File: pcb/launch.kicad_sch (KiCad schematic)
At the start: 243 parts, among them J1 DNP, J6 DNP, U1 AT90USB646-MUR, Y0 ECS-160-18-23G-JGN-TR

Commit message: work in progress toward 2.0
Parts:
- added J7: FH12-16S-0.5SH(55), Connector_FFC-FPC:Hirose_FH12-16S-0.5SH_1x16-1MP_P0.50mm_Horizontal, symbol Connector_Generic_MountingPin:Conn_01x16_MountingPin
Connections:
- net +3V6: now also J7.14 (Pin_14), J7.15 (Pin_15)
- net COLD: now also J7.12 (Pin_12)
- net COLE: now also J7.11 (Pin_11)
- net COLF: now also J7.10 (Pin_10)
- net COLM: now also J7.9 (Pin_9)
- net GND: now also J7.1 (Pin_1), J7.16 (Pin_16), J7.8 (Pin_8), J7.MP (MountPin)
- net LED_TEN: now reaches LO0.3 (DOUT)
- net LED_TEN: now also J7.13 (Pin_13)
- net ROW6: now reaches U1.27 (PD2)
- net ROW6: now also J7.2 (Pin_2)
- net ROW7: now reaches U1.29 (PD4)
- net ROW7: now also J7.3 (Pin_3)
- net ROW8: now reaches U1.30 (PD5)
- net ROW8: now also J7.4 (Pin_4)
- net ROW9: now reaches U1.31 (PD6)
- net ROW9: now also J7.5 (Pin_5)
- net ROW10: now reaches U1.32 (PD7)
- net ROW10: now also J7.6 (Pin_6)
- net ROW11: now reaches U1.33 (PE0)
- net ROW11: now also J7.7 (Pin_7)
- no-connect marks 3 -> 2
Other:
- sheet power ports: added none; removed ~{RESET}
- note added: "Tenkey connector"

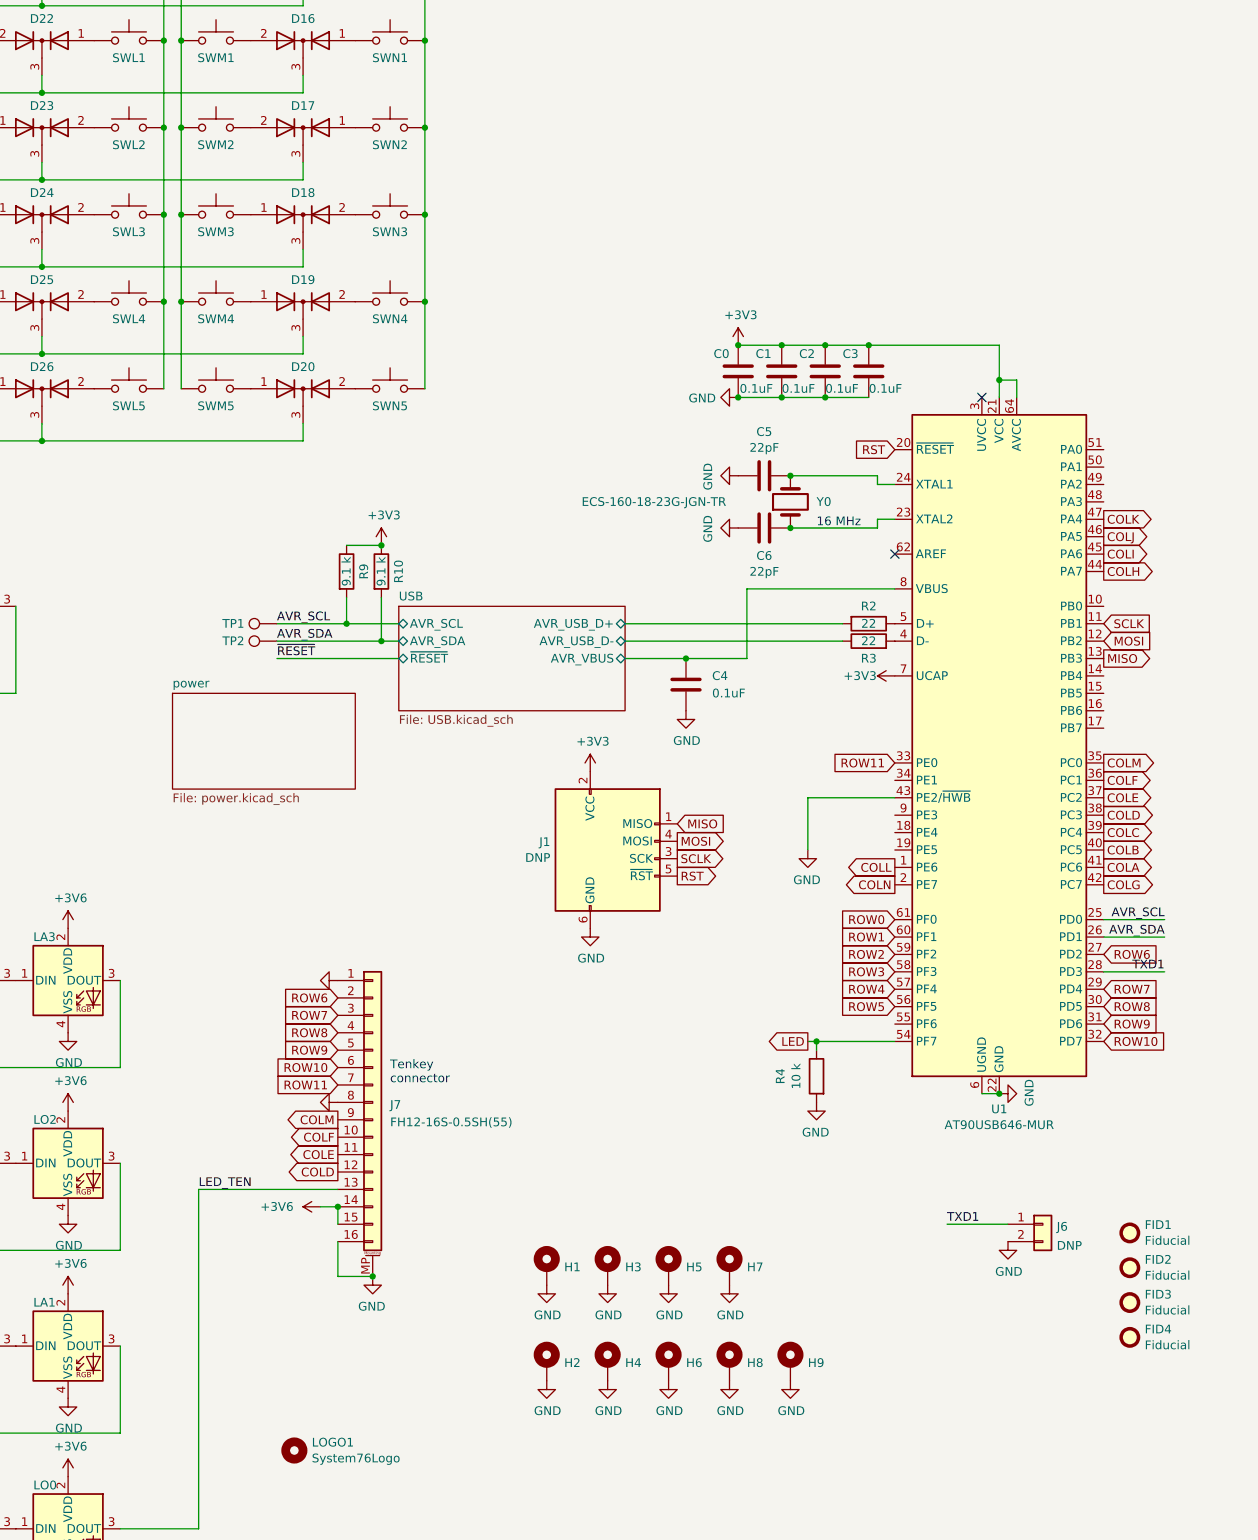
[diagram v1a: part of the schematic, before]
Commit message: version pins, finalize routing FFC connector changed to 20 pin USB hub reset pull down via stitching route remaining nets and cleanup
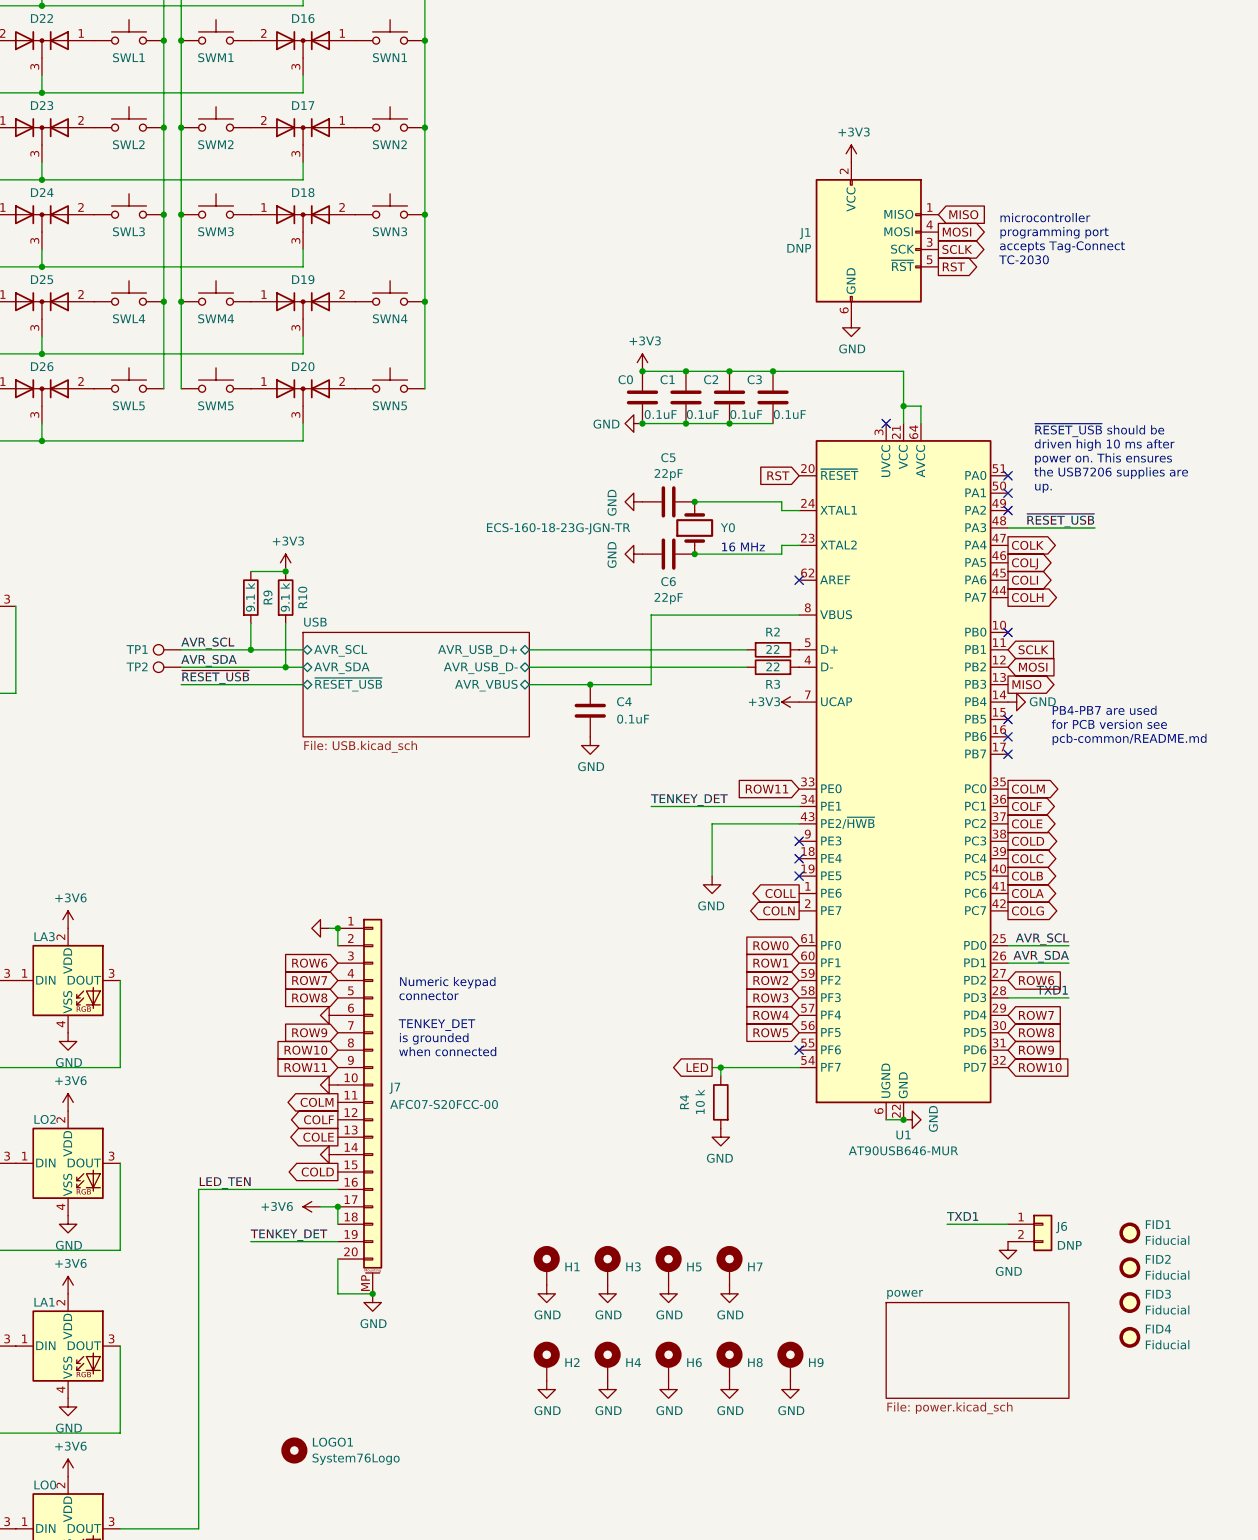
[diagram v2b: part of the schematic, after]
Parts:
- removed J7: FH12-16S-0.5SH(55), Connector_FFC-FPC:Hirose_FH12-16S-0.5SH_1x16-1MP_P0.50mm_Horizontal, symbol Connector_Generic_MountingPin:Conn_01x16_MountingPin
- added J7: AFC07-S20FCC-00, launch:AFC07-S20FCC-00, symbol Connector_Generic_MountingPin:Conn_01x20_MountingPin
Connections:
- net +3V6: now also J7.17 (Pin_17), J7.18 (Pin_18)
- net COLD: now also J7.15 (Pin_15)
- net COLE: now also J7.13 (Pin_13)
- net COLF: now also J7.12 (Pin_12)
- net COLM: now also J7.11 (Pin_11)
- net GND: now also U1.14 (PB4), J7.1 (Pin_1), J7.10 (Pin_10), J7.14 (Pin_14), J7.2 (Pin_2), J7.20 (Pin_20), J7.6 (Pin_6), J7.MP (MountPin)
- net LED_TEN: now also J7.16 (Pin_16)
- net ROW10: now also J7.8 (Pin_8)
- net ROW11: now also J7.9 (Pin_9)
- net ROW6: now also J7.3 (Pin_3)
- net ROW7: now also J7.4 (Pin_4)
- net ROW8: now also J7.5 (Pin_5)
- net ROW9: now also J7.7 (Pin_7)
- net TENKEY_DET: now reaches U1.34 (PE1)
- net TENKEY_DET: now also J7.19 (Pin_19)
- net ~{RESET_USB}: now reaches U1.48 (PA3)
- no-connect marks 2 -> 13
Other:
- sheet USB ports: added ~{RESET_USB}; removed ~{RESET}
- note added: "Numeric keypad connector TENKEY_DET is grounded when connected"
- note added: "PB4-PB7 are used for PCB version see pcb-common/README.md"
- note added: "microcontroller programming port accepts Tag-Connect TC-2030"
- note added: "~{RESET_USB} should be driven high 10 ms after power on. This ensures the USB7206 supplies are up."
- note removed: "Tenkey connector"
- moved on the sheet: C0, C1, C2, C3, C4, C5, C6, J1, R10, R2, R3, R4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

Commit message: set versions
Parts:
- J7: Manufacturer (none) -> Jushou
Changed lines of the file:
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@@
   (title_block
     (title "Launch")
-    (date "2022-05-19")
-    (rev "pre-2.0")
+    (date "2022-05-23")
+    (rev "2.0")
     (company "System76")
   )
@@
     (stroke (width 0) (type default) (color 0 0 0 0))
   )
-  (wire (pts (xy 384.81 190.5) (xy 375.92 190.5))
+  (wire (pts (xy 388.62 190.5) (xy 375.92 190.5))
     (stroke (width 0) (type default) (color 0 0 0 0))
   )
@@
     (effects (font (size 1.27 1.27)) (justify right bottom))
   )
-  (label "TXD1" (at 384.81 190.5 180)
+  (label "TXD1" (at 388.62 190.5 180)
     (effects (font (size 1.27 1.27)) (justify right bottom))
   )
@@
       (effects (font (size 1.27 1.27)) hide)
     )
+    (property "Manufacturer" "Jushou" (id 4) (at 283.21 203.2 0)
+      (effects (font (size 1.27 1.27)) hide)
+    )
